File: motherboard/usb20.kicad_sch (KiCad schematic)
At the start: 19 parts, among them J16 USB, J17 USB, J18 USB, J19 USB, U22 CH334F, Y2 12MHz

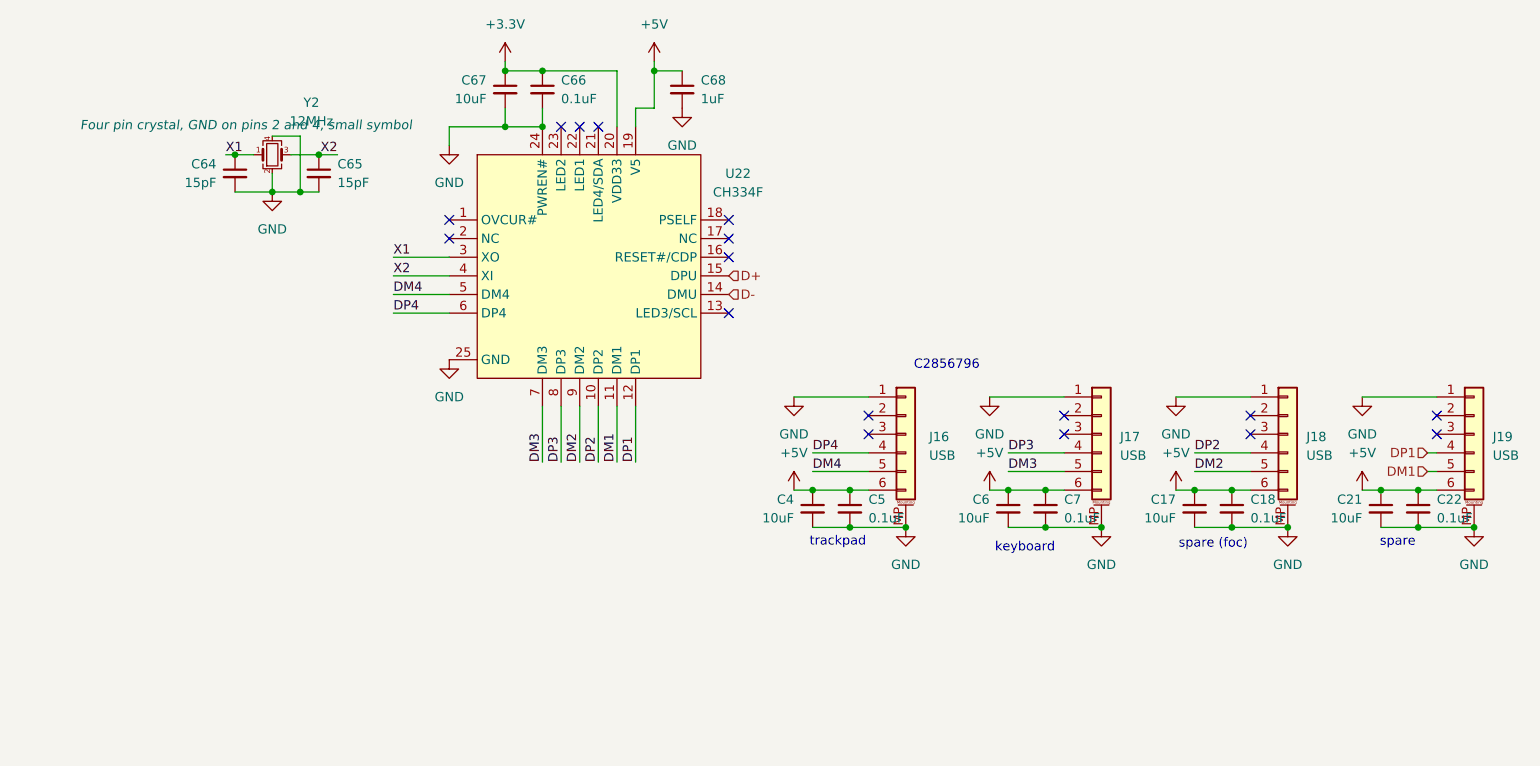
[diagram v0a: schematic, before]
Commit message: v0.2 good routing checkpoint (217 unrouted)
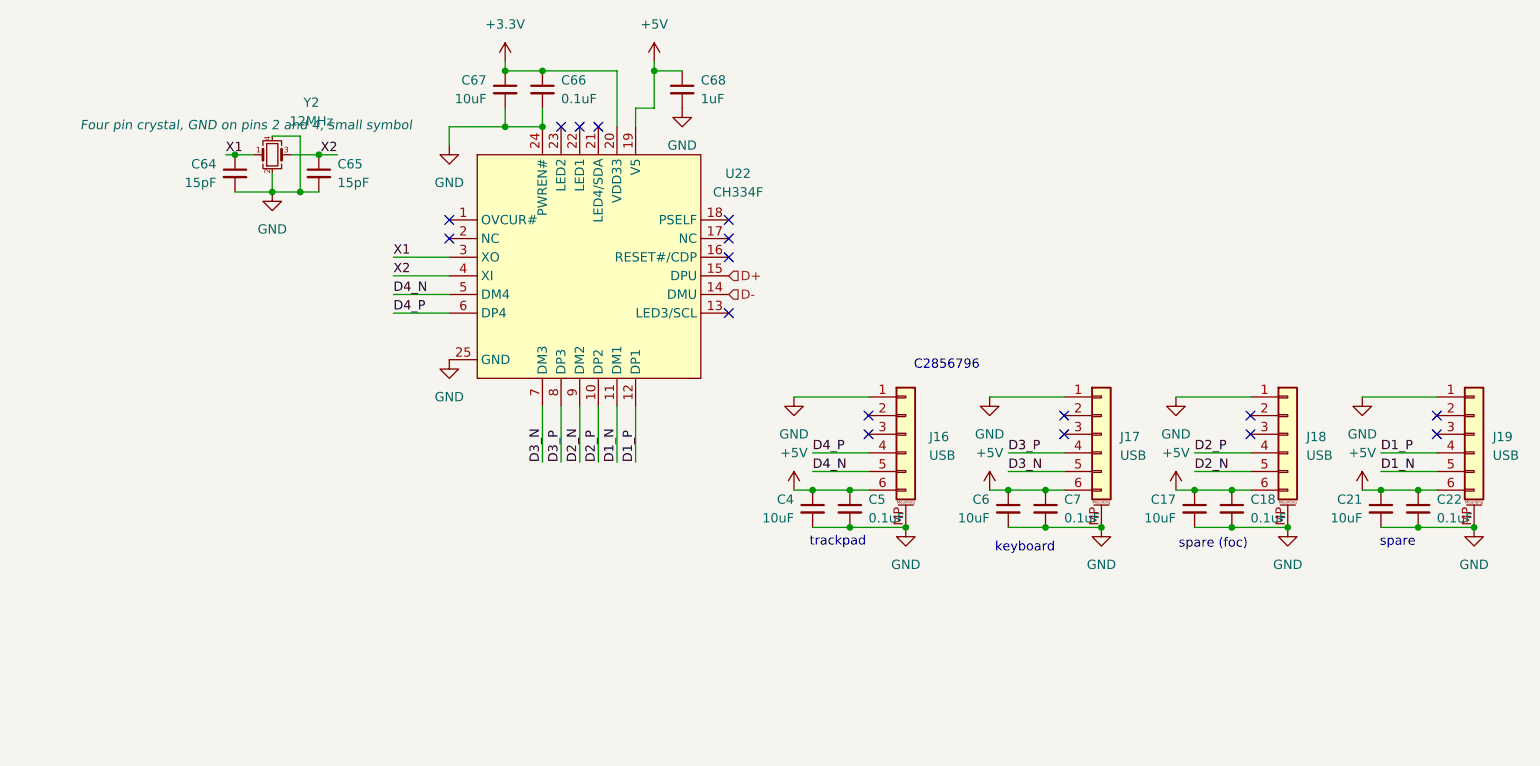
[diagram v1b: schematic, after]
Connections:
- net DM1 renamed D1_N
- net DM2 renamed D2_N
- net DM3 renamed D3_N
- net DM4 renamed D4_N
- net DP1 renamed D1_P
- net DP2 renamed D2_P
- net DP3 renamed D3_P
- net DP4 renamed D4_P
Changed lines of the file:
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@@
 	(wire
 		(pts
-			(xy 233.68 115.57) (xy 234.95 115.57)
+			(xy 227.33 115.57) (xy 234.95 115.57)
 		)
 		(stroke
@@
 	(wire
 		(pts
-			(xy 233.68 113.03) (xy 234.95 113.03)
+			(xy 227.33 113.03) (xy 234.95 113.03)
 		)
 		(stroke
@@
 		)
 	)
-	(label "DP4"
+	(label "D4_P"
 		(at 92.71 93.98 0)
 		(fields_autoplaced yes)
@@
 		)
 	)
-	(label "DM4"
+	(label "D4_N"
 		(at 92.71 91.44 0)
 		(fields_autoplaced yes)
@@
 		)
 	)
-	(label "DM2"
+	(label "D2_N"
 		(at 118.11 114.3 90)
 		(fields_autoplaced yes)
@@
 		)
 	)
-	(label "DP3"
+	(label "D1_P"
+		(at 227.33 113.03 0)
+		(fields_autoplaced yes)
+		(effects
+			(font
+				(size 1.27 1.27)
+			)
+			(justify left bottom)
+		)
+	)
+	(label "D3_P"
 		(at 115.57 114.3 90)
 		(fields_autoplaced yes)
@@
 		)
 	)
-	(label "DM4"
+	(label "D4_N"
 		(at 149.86 115.57 0)
 		(fields_autoplaced yes)
@@
 		)
 	)
-	(label "DP2"
+	(label "D2_P"
 		(at 120.65 114.3 90)
 		(fields_autoplaced yes)
@@
 		)
 	)
-	(label "DP2"
+	(label "D2_P"
 		(at 201.93 113.03 0)
 		(fields_autoplaced yes)
@@
 		)
 	)
-	(label "DP3"
+	(label "D1_N"
+		(at 227.33 115.57 0)
+		(fields_autoplaced yes)
+		(effects
+			(font
+				(size 1.27 1.27)
+			)
+			(justify left bottom)
+		)
+	)
+	(label "D3_P"
 		(at 176.53 113.03 0)
 		(fields_autoplaced yes)
@@
 		)
 	)
-	(label "DM1"
+	(label "D1_N"
 		(at 123.19 114.3 90)
 		(fields_autoplaced yes)
@@
 		)
 	)
-	(label "DM2"
+	(label "D2_N"
 		(at 201.93 115.57 0)
 		(fields_autoplaced yes)
@@
 		)
 	)
-	(label "DP1"
+	(label "D1_P"
 		(at 125.73 114.3 90)
 		(fields_autoplaced yes)
@@
 		)
 	)
-	(label "DP4"
+	(label "D4_P"
 		(at 149.86 113.03 0)
 		(fields_autoplaced yes)
@@
 		)
 	)
-	(label "DM3"
+	(label "D3_N"
 		(at 176.53 115.57 0)
 		(fields_autoplaced yes)
@@
 		)
 	)
-	(label "DM3"
+	(label "D3_N"
 		(at 113.03 114.3 90)
 		(fields_autoplaced yes)
@@
 		)
 	)
-	(hierarchical_label "DM1"
-		(shape input)
-		(at 233.68 115.57 180)
-		(fields_autoplaced yes)
-		(effects
-			(font
-				(size 1.27 1.27)
-			)
-			(justify right)
-		)
-	)
 	(hierarchical_label "D+"
 		(shape input)
@@
 		)
 	)
-	(hierarchical_label "DP1"
-		(shape input)
-		(at 233.68 113.03 180)
-		(fields_autoplaced yes)
-		(effects
-			(font
-				(size 1.27 1.27)
-			)
-			(justify right)
-		)
-	)

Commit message: mainboard v0.3 + power WIP
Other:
- company: (none) -> Byran Huang
- title: (none) -> anyon e
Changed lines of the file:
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@@
 	(generator_version "8.99")
 	(paper "A4")
+	(title_block
+		(title "anyon e")
+		(date "2024-09-15")
+		(rev "V0.3")
+		(company "Byran Huang")
+		(comment 4 "Proof of concept board for feature verification")
+	)
 	(text "trackpad"
 		(exclude_from_sim no)

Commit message: preparing for motherboard v1.1
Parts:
- renumbered C67 to C60, C66 to C61, C68 to C62, C64 to C63, C65 to C64, C4 to C65, C5 to C66, C6 to C67, C7 to C68, C17 to C69, C18 to C70, C21 to C71, C22 to C72, J16 to J19, J17 to J20, J18 to J21, J19 to J22, U22 to U20, Y2 to Y1
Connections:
- net D3_N: no longer J20.5 (Pin_5)
- net D3_P: no longer J20.4 (Pin_4)
- new net EXTUSB20_D3_N: J20.5 (Pin_5)
- new net EXTUSB20_D3_P: J20.4 (Pin_4)
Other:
- moved on the sheet: C67, C68, J20
